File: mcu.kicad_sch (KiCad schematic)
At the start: 35 parts, among them J2 SWD, J3 SWC, U1 NRF52840-QIAA-R, Y1 ECS-.327-9-34B-TR, Y2 XRCGB32M000F1S2KR0

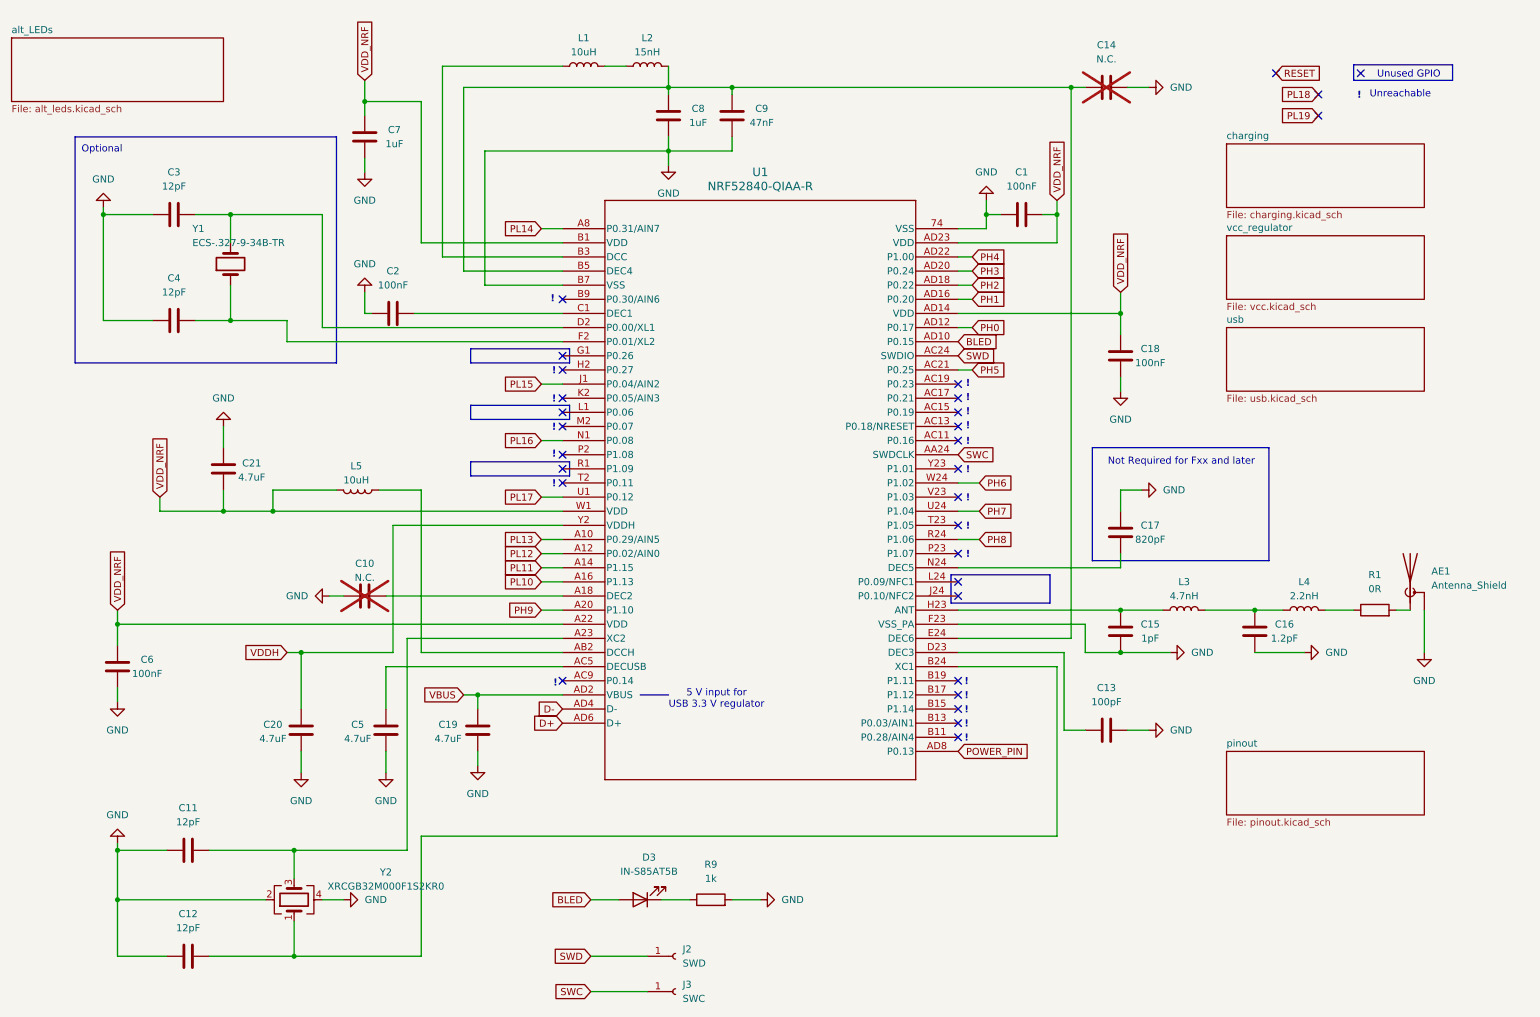
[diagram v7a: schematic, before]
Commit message: Replaced IC with NINA Module
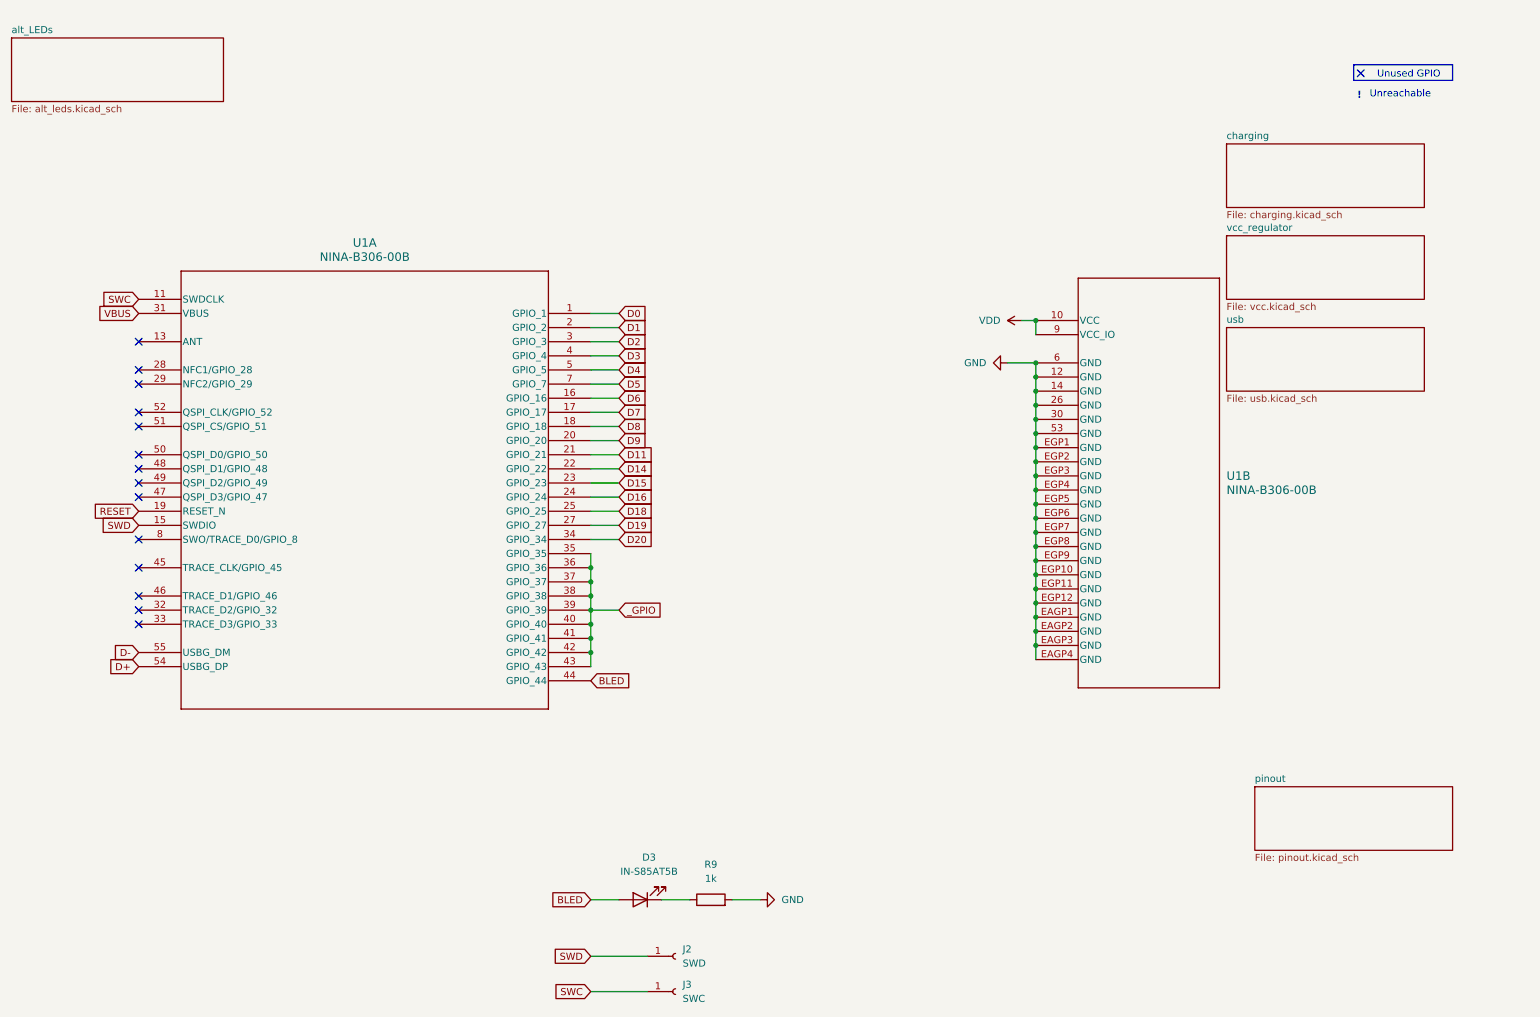
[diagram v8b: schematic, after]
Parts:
- removed AE1: Antenna_Shield, Antenna:2.4GHz F Antenna, symbol Device:Antenna_Shield
- removed C1, C18, C2, C6: 100nF, Capacitor_SMD:C_0402_1005Metric, symbol Device:C
- removed C10, C14: N.C., Capacitor_SMD:C_0402_1005Metric, symbol Device:C
- removed C11, C12, C3, C4: 12pF, Capacitor_SMD:C_0402_1005Metric, symbol Device:C
- removed C13: 100pF, Capacitor_SMD:C_0402_1005Metric, symbol Device:C
- removed C15: 1pF, Capacitor_SMD:C_0402_1005Metric, symbol Device:C
- removed C16: 1.2pF, Capacitor_SMD:C_0402_1005Metric, symbol Device:C
- removed C17: 820pF, Capacitor_SMD:C_0402_1005Metric, symbol Device:C
- removed C19, C20, C21, C5: 4.7uF, Capacitor_SMD:C_0603_1608Metric, symbol Device:C
- removed C7, C8: 1uF, Capacitor_SMD:C_0603_1608Metric, symbol Device:C
- removed C9: 47nF, Capacitor_SMD:C_0402_1005Metric, symbol Device:C
- removed L1, L5: 10uH, Inductor_SMD:L_0603_1608Metric, symbol Device:L
- removed L2: 15nH, Inductor_SMD:L_0402_1005Metric, symbol Device:L
- removed L3: 4.7nH, Inductor_SMD:L_0402_1005Metric, symbol Device:L
- removed L4: 2.2nH, Inductor_SMD:L_0402_1005Metric, symbol Device:L
- removed R1: 0R, Resistor_SMD:R_0402_1005Metric_Pad0.72x0.64mm_HandSolder, symbol Device:R
- removed U1: NRF52840-QIAA-R, NRF52840-QIAA-R:AQFN73_7X7_NOR, symbol NRF52840-QIAA-R:NRF52840-QIAA-R
- removed Y1: ECS-.327-9-34B-TR, Crystal:Crystal_SMD_3215-2Pin_3.2x1.5mm, symbol Device:Crystal
- removed Y2: XRCGB32M000F1S2KR0, Crystal:Crystal_SMD_2016-4Pin_2.0x1.6mm, symbol Device:Crystal_GND24
- added U1: NINA-B306-00B, NINA_B306_00B:NINA-B3x6_UBL, symbol 2026-03-14_18-43-27:NINA-B306-00B
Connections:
- net BLED: now also U1.44 (GPIO_44)
- net D+: now also U1.54 (USBG_DP)
- net D-: now also U1.55 (USBG_DM)
- net GND: now also U1.12 (GND), U1.14 (GND), U1.26 (GND), U1.30 (GND), U1.53 (GND), U1.6 (GND), U1.EAGP1 (GND), U1.EAGP2 (GND), U1.EAGP3 (GND), U1.EAGP4 (GND), U1.EGP1 (GND), U1.EGP10 (GND), U1.EGP11 (GND), U1.EGP12 (GND), U1.EGP2 (GND), U1.EGP3 (GND), U1.EGP4 (GND), U1.EGP5 (GND), U1.EGP6 (GND), U1.EGP7 (GND), U1.EGP8 (GND), U1.EGP9 (GND)
- net RESET: now also U1.19 (RESET_N)
- net SWC: now also U1.11 (SWDCLK)
- net SWD: now also U1.15 (SWDIO)
- net VBUS: now also U1.31 (VBUS)
- new net D0: U1.1 (GPIO_1)
- new net D1: U1.2 (GPIO_2)
- new net D11: U1.21 (GPIO_21)
- new net D14: U1.22 (GPIO_22)
- new net D15: U1.23 (GPIO_23)
- new net D16: U1.24 (GPIO_24)
- new net D18: U1.25 (GPIO_25)
- new net D19: U1.27 (GPIO_27)
- new net D2: U1.3 (GPIO_3)
- new net D20: U1.34 (GPIO_34)
- new net D3: U1.4 (GPIO_4)
- new net D4: U1.5 (GPIO_5)
- new net D5: U1.7 (GPIO_7)
- new net D6: U1.16 (GPIO_16)
- new net D7: U1.17 (GPIO_17)
- new net D8: U1.18 (GPIO_18)
- new net D9: U1.20 (GPIO_20)
- new net VDD: U1.10 (VCC), U1.9 (VCC_IO)
- new net _GPIO: U1.35 (GPIO_35), U1.36 (GPIO_36), U1.37 (GPIO_37), U1.38 (GPIO_38), U1.39 (GPIO_39), U1.40 (GPIO_40), U1.41 (GPIO_41), U1.42 (GPIO_42), U1.43 (GPIO_43)
- no-connect marks 30 -> 15
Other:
- note removed: "5 V input for USB 3.3 V regulator"
- note removed: "Not Required for Fxx and later"
- note removed: "Optional"
